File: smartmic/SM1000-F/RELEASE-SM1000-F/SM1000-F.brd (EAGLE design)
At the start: 65 x 100 mm, 216 parts, among them CN1 HDR100-3, CN10 ST-3509, CN11 HDR100-3, CN12 DIL16X300, CN2 JS-MU3-002, CN3 DS-0518, CN4 RJ-45, CN5 ST-3509, CN6 ST-3509, CN7 ST-3509, CN8 ST-3509, CN9 ST-3509, J1 JMP-2PIN, J2 JMP-2PIN, J3 JMP-2PIN, J4 CONN-BOOM-XH-2A, J5 JMP-2PIN, P1 TPAD50, P10 TPAD50, P11 TPAD50, P12 TPAD50, P13 TPAD50, P14 TPAD50, P15 TPAD50, P16 TPAD50, P17 TPAD50, P18 TPAD50, P19 TPAD50, P2 TPAD50, P20 TPAD50, P21 TPAD50, P3 TPAD50, P4 TPAD50, P5 TPAD50, P6 TPAD50, P7 TPAD50, P8 TPAD50, P9 TPAD50, SW1 SW-LC2259, SW2 TS-026, SW3 SW-LC2259EENP, SW4 TS-026, SW5 TS-02B, T1 SM-LP-5001, T2 SM-LP-5001, U1 STM32F405VGT6, U10 DNL, U2 LD3985M33R, U3 STMPS2141, U4 EMIF02-USB03F2, U5 TPS54329E, U6 LMV341, U7 LMV341, U8 LM386M-1, U9 LMV341

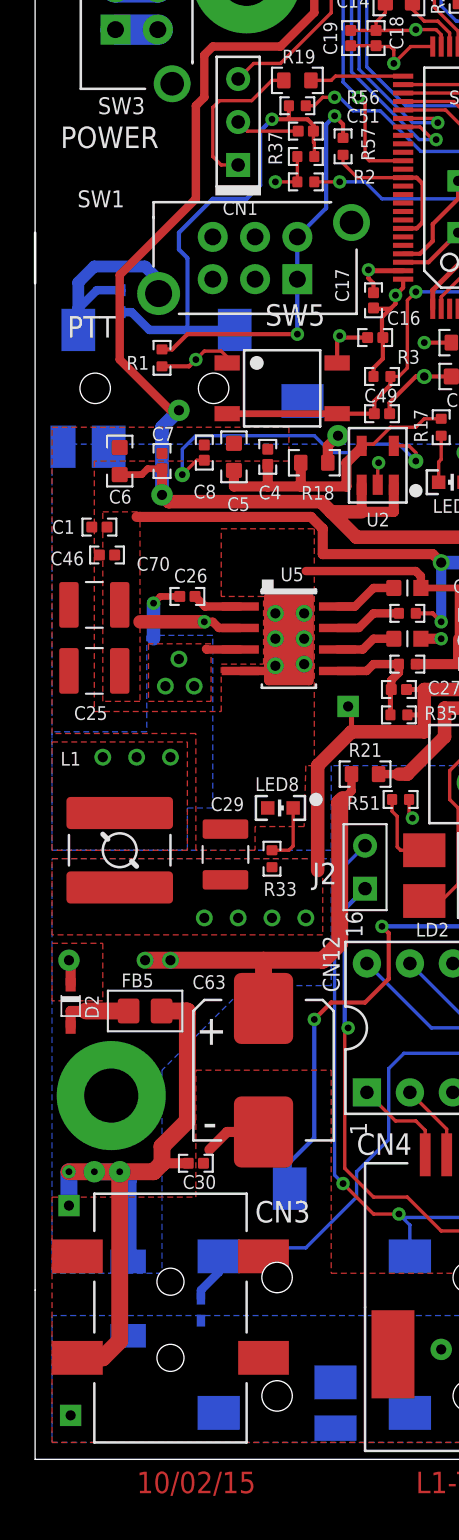
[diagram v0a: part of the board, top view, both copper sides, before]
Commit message: removed GNDs from SW1 & SW3 mounting tabs
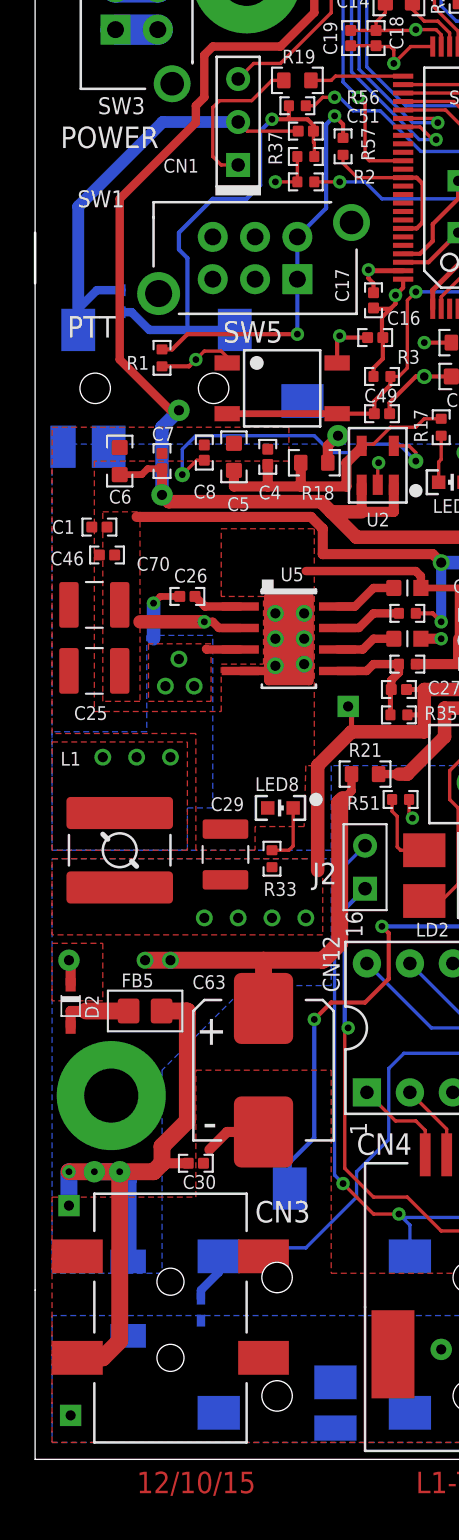
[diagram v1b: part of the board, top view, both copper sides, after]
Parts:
- moved DRILEGEND 4.12 mm to (21.3, -14.2)
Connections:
- net GND: no longer SW1.7, SW1.8, SW3.7, SW3.8
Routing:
- net GND: track 230.1 -> 240.5 mm
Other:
- board text added: "12/10/15"
- board text added: "SM1000-F 12/11/15 RGB."
- board text removed: "10/02/15"
- board text removed: "SM1000-F 10/03/15 RGB."
